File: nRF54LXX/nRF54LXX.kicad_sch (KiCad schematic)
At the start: 24 parts, among them IC1 NRF54L15-QFAA-R7, J1 MM8130-2600RA2, J2 Programmer, Y1 32.768kHz, Y2 32MHz

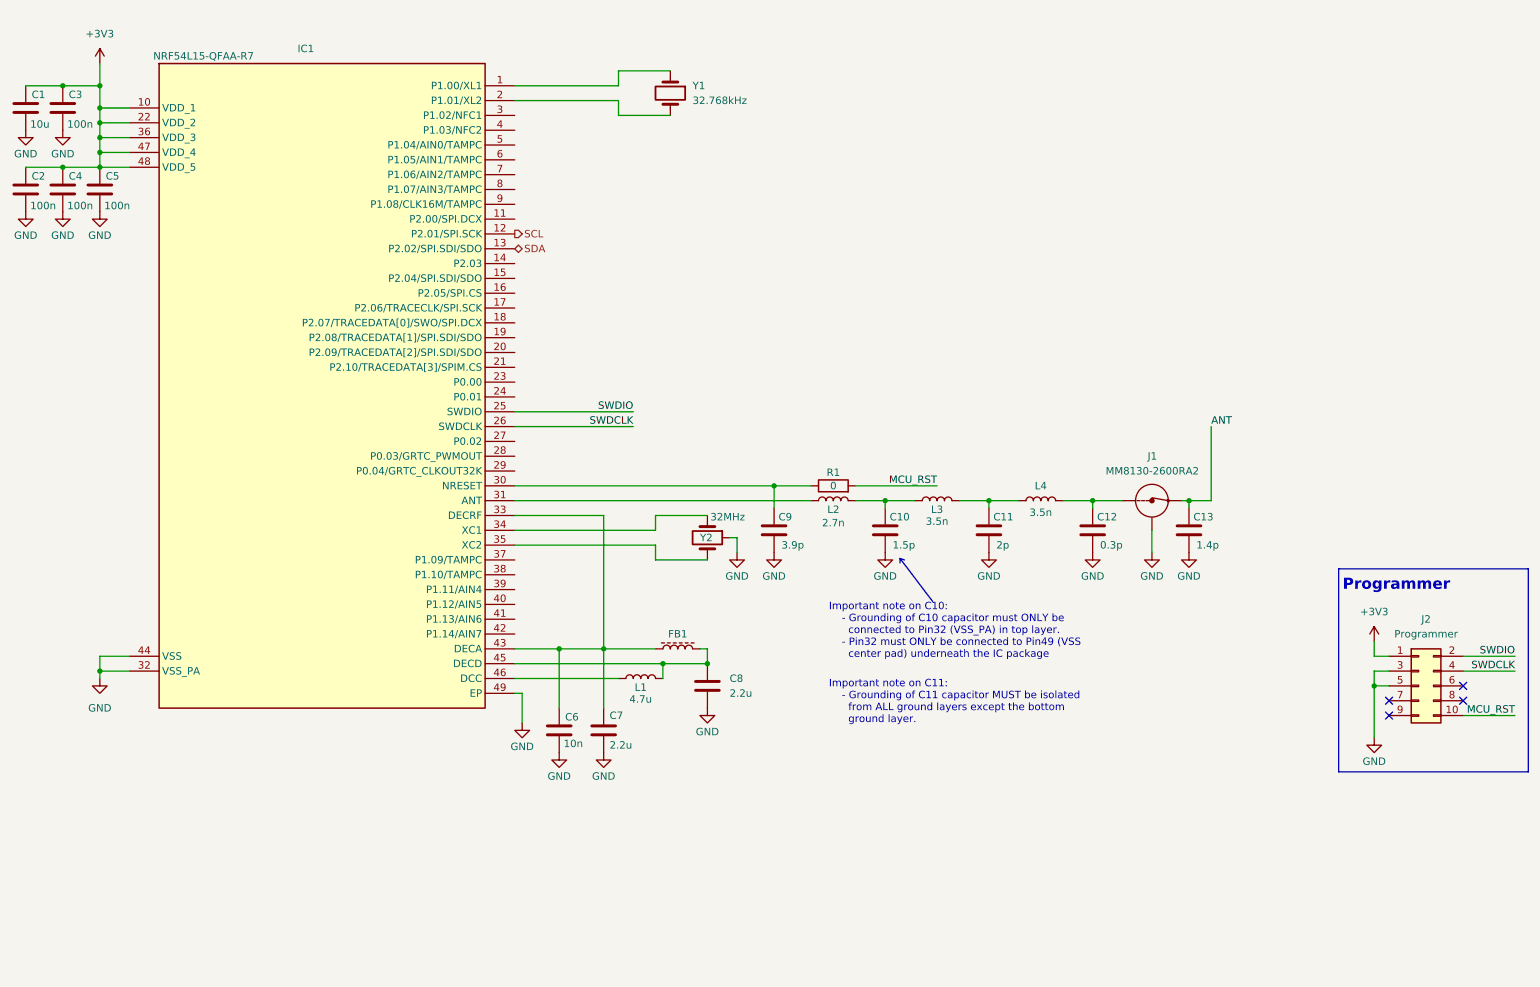
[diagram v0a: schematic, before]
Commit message: Updated Schematic to increase readability
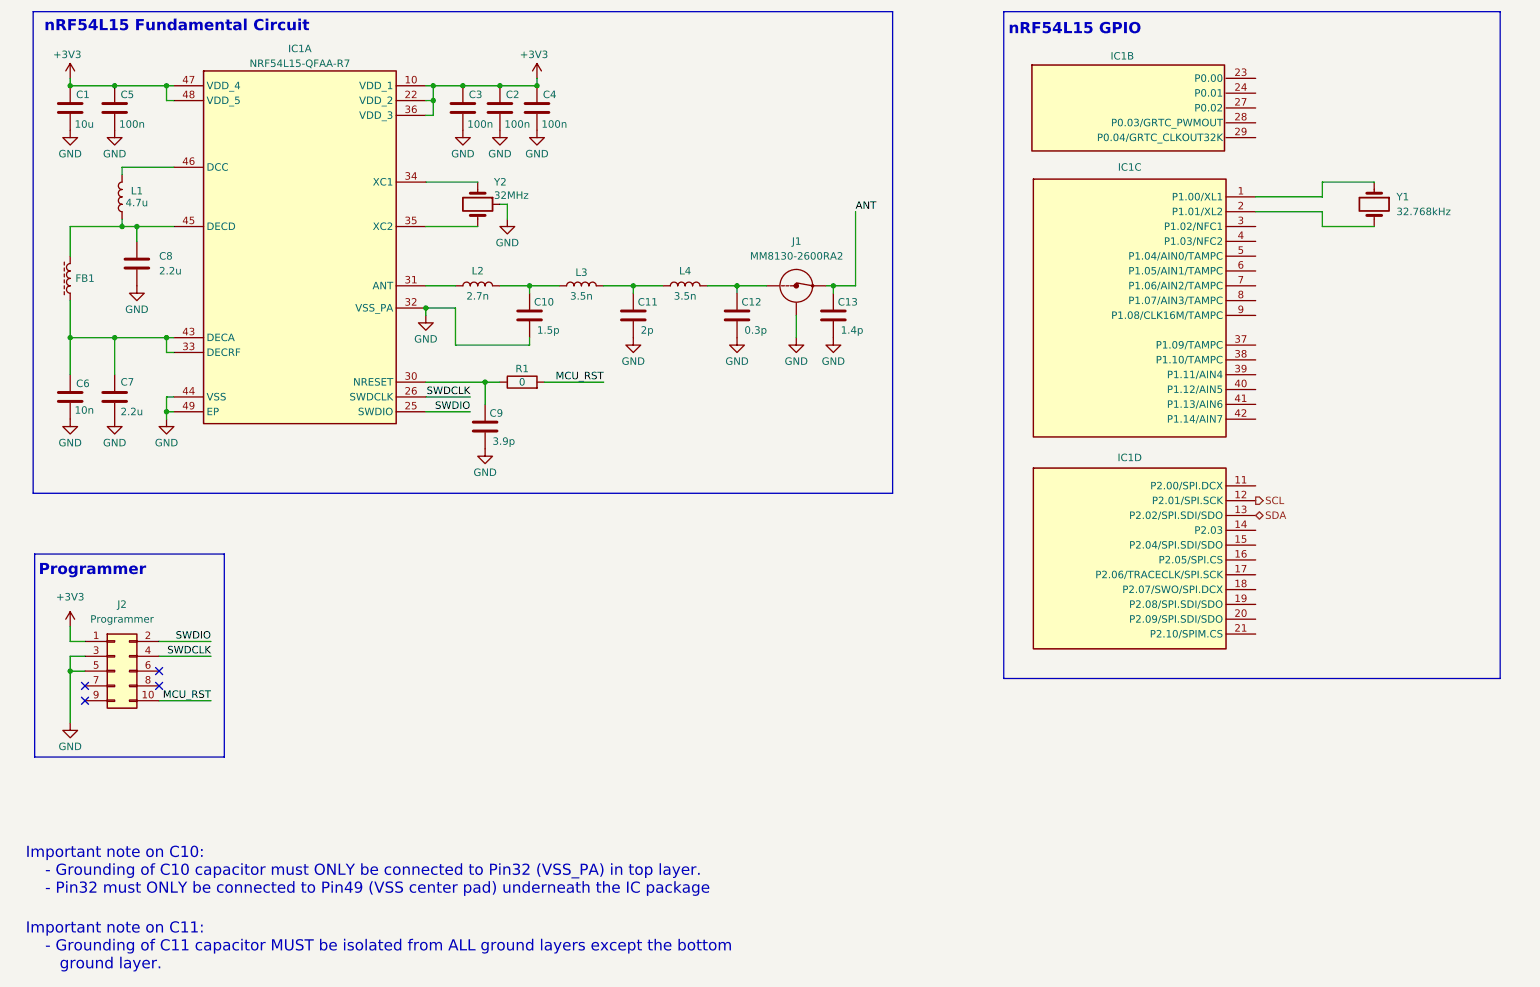
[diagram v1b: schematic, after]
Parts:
- removed IC1: NRF54L15-QFAA-R7, Qoves:QFN40P600X600X90-49N-D, symbol NRF54L15-QFAA-R7:NRF54L15-QFAA-R7
- added IC1: NRF54L15-QFAA-R7, Qoves:QFN40P600X600X90-49N-D, symbol nrf54l15-qfaa-r7:NRF54L15-QFAA-R7
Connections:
- net +3V3: now also IC1.10 (VDD_1), IC1.22 (VDD_2), IC1.36 (VDD_3), IC1.47 (VDD_4), IC1.48 (VDD_5)
- net GND: now also IC1.32 (VSS_PA), IC1.44 (VSS), IC1.49 (EP)
- net SCL: now also IC1.12 (P2.01/SPI.SCK)
- net SDA: now also IC1.13 (P2.02/SPI.SDI/SDO)
- net SWDCLK: now also IC1.26 (SWDCLK)
- net SWDIO: now also IC1.25 (SWDIO)
- net at L2.2: now also IC1.31 (ANT)
- net at C8.1, FB1.2: now also L1.2, IC1.45 (DECD); no longer L1.1
- net at Y2.1: now also IC1.34 (XC1)
- net at Y2.3: now also IC1.35 (XC2)
- net at C9.1, R1.1: now also IC1.30 (NRESET)
- net at C6.1, C7.1, FB1.1: now also IC1.33 (DECRF), IC1.43 (DECA)
- net at Y1.1: now also IC1.1 (P1.00/XL1)
- net at Y1.2: now also IC1.2 (P1.01/XL2)
- new net: IC1.46 (DCC), L1.1
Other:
- note added: "nRF54L15 Fundamental Circuit"
- note added: "nRF54L15 GPIO"
- company: (none) -> By C.S
- title: (none) -> nRF54L15
- moved on the sheet: C1, C10, C11, C12, C13, C2, C3, C4, C5, C6, C7, C8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
